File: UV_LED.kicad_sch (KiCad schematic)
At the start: 39 parts, among them IC1 IS31LT3178-GRLS4-TR, J1 Conn_01x04, J2 Conn_01x04

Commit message: added kicad files
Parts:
- removed D13, D16, D17, D18, D19, D6: LED, symbol Device:LED
- removed U?: (no value), symbol LED:CN5501
- removed U?: CN5501, symbol LED:CN5501
- added Q1, Q2: Q_NMOS_GDS, Package_TO_SOT_SMD:SOT-23, symbol Device:Q_NMOS_GDS
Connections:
- net at D5.1 (K), R2.1: now also Q1.2 (D)
- net at C1.1, IC1.1 (OUT_1), IC1.2 (OUT_2): now also Q1.3 (S), Q2.3 (S)
- net at D12.1 (K): now also Q2.2 (D)
- net at R1.2: now also Q1.1 (G)
- net at R2.2: now also Q2.1 (G)

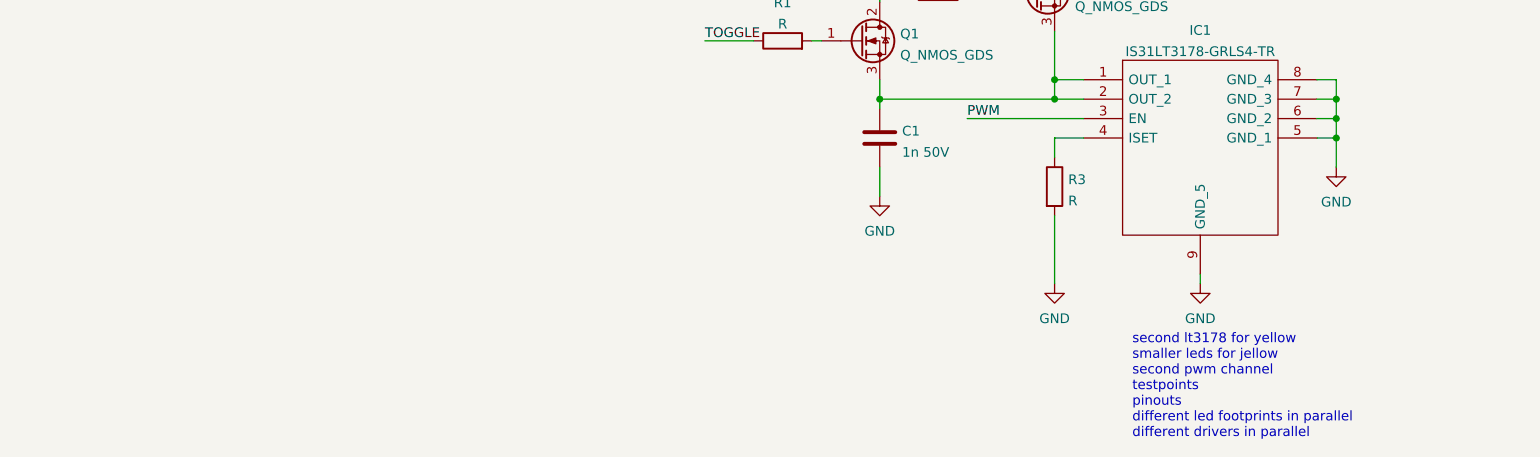
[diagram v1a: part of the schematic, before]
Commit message: added TX6120, CN5501 and AL8861
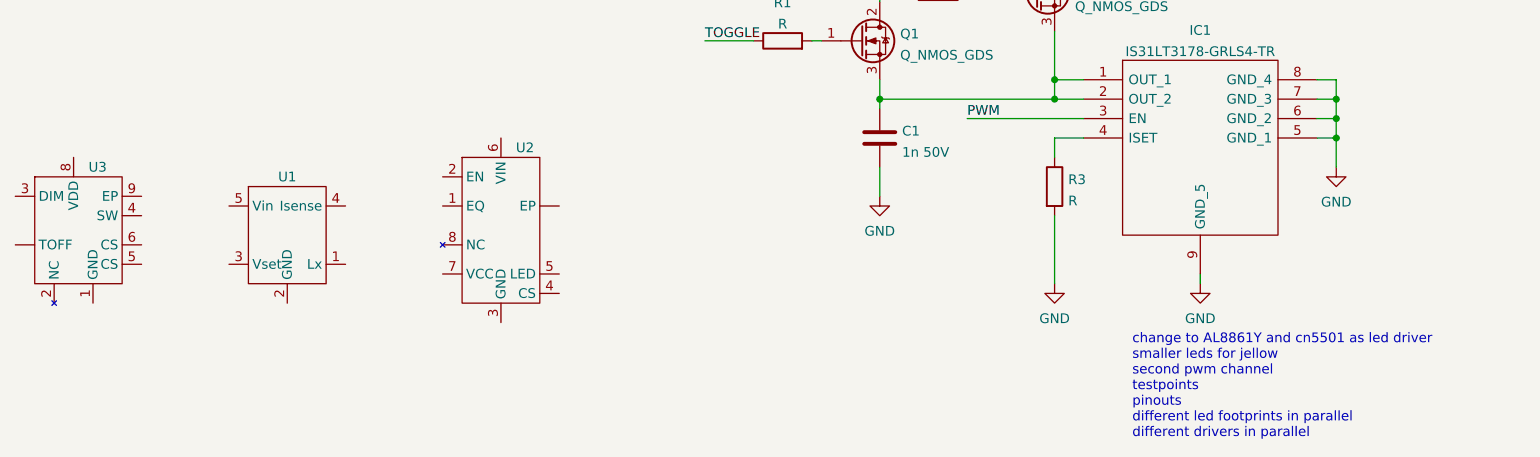
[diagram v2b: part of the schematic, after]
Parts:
- added U1: ~, symbol 1_meins:AL8861
- added U2: ~, symbol 1_meins:CN5501
- added U3: ~, symbol 1_meins:TX6120
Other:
- note added: "change to AL8861Y and cn5501 as led driver smaller leds for jellow second pwm channel testpoints pinouts different led footprints in parallel different drivers in parallel"
- note removed: "second lt3178 for yellow smaller leds for jellow second pwm channel testpoints pinouts different led footprints in parallel different drivers in parallel"

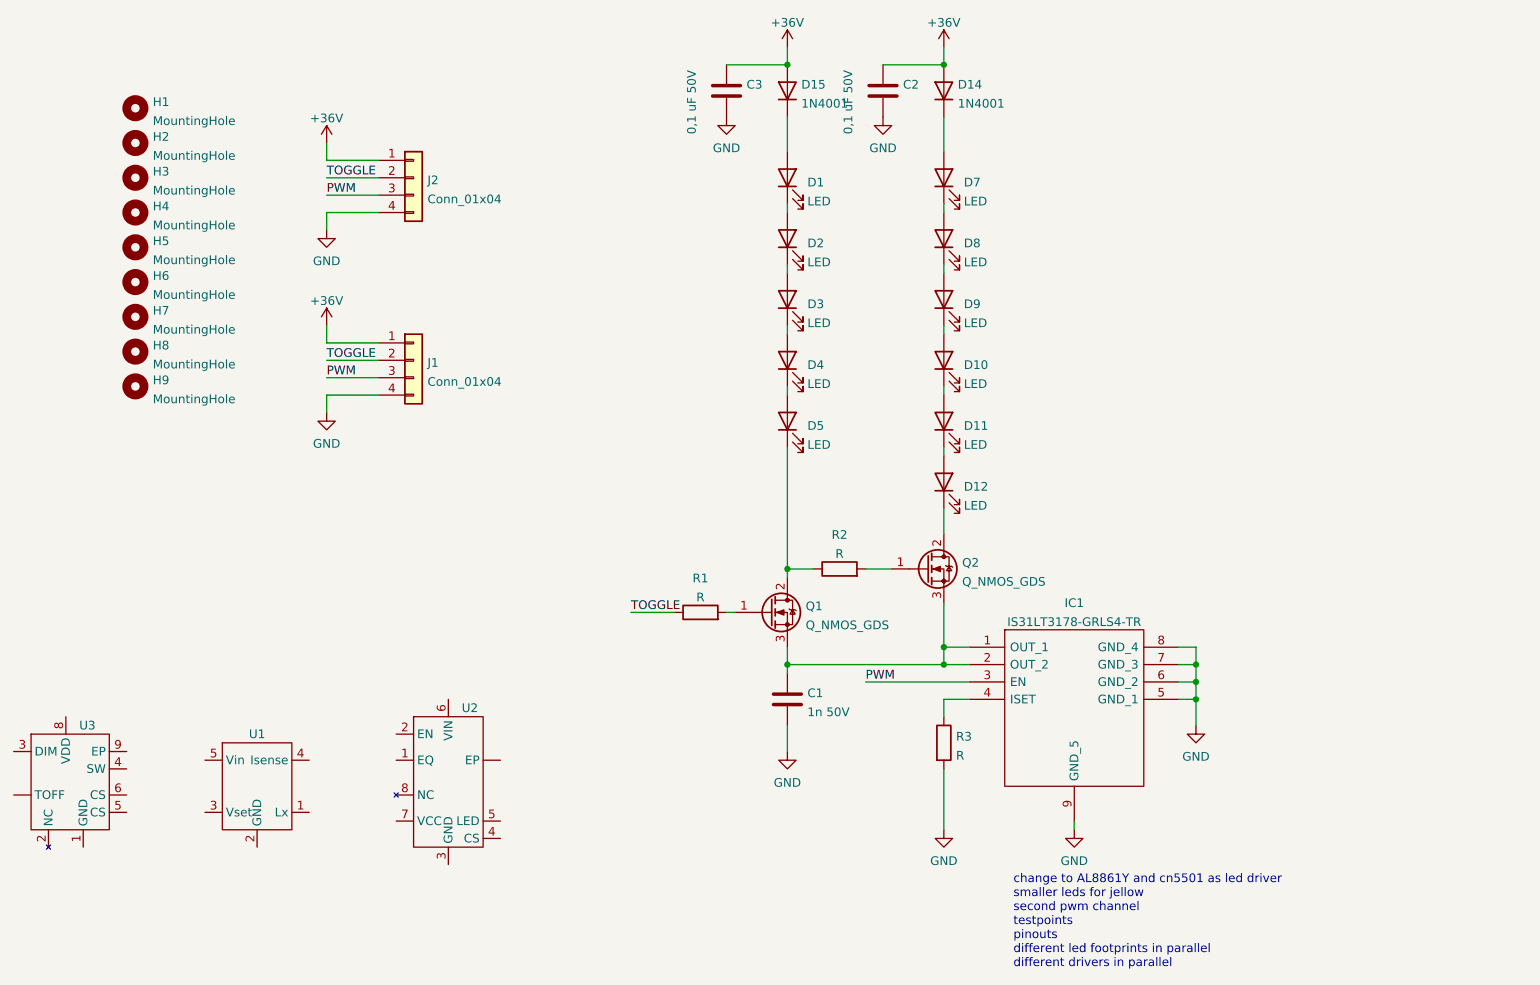
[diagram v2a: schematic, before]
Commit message: sheet for new LED driver
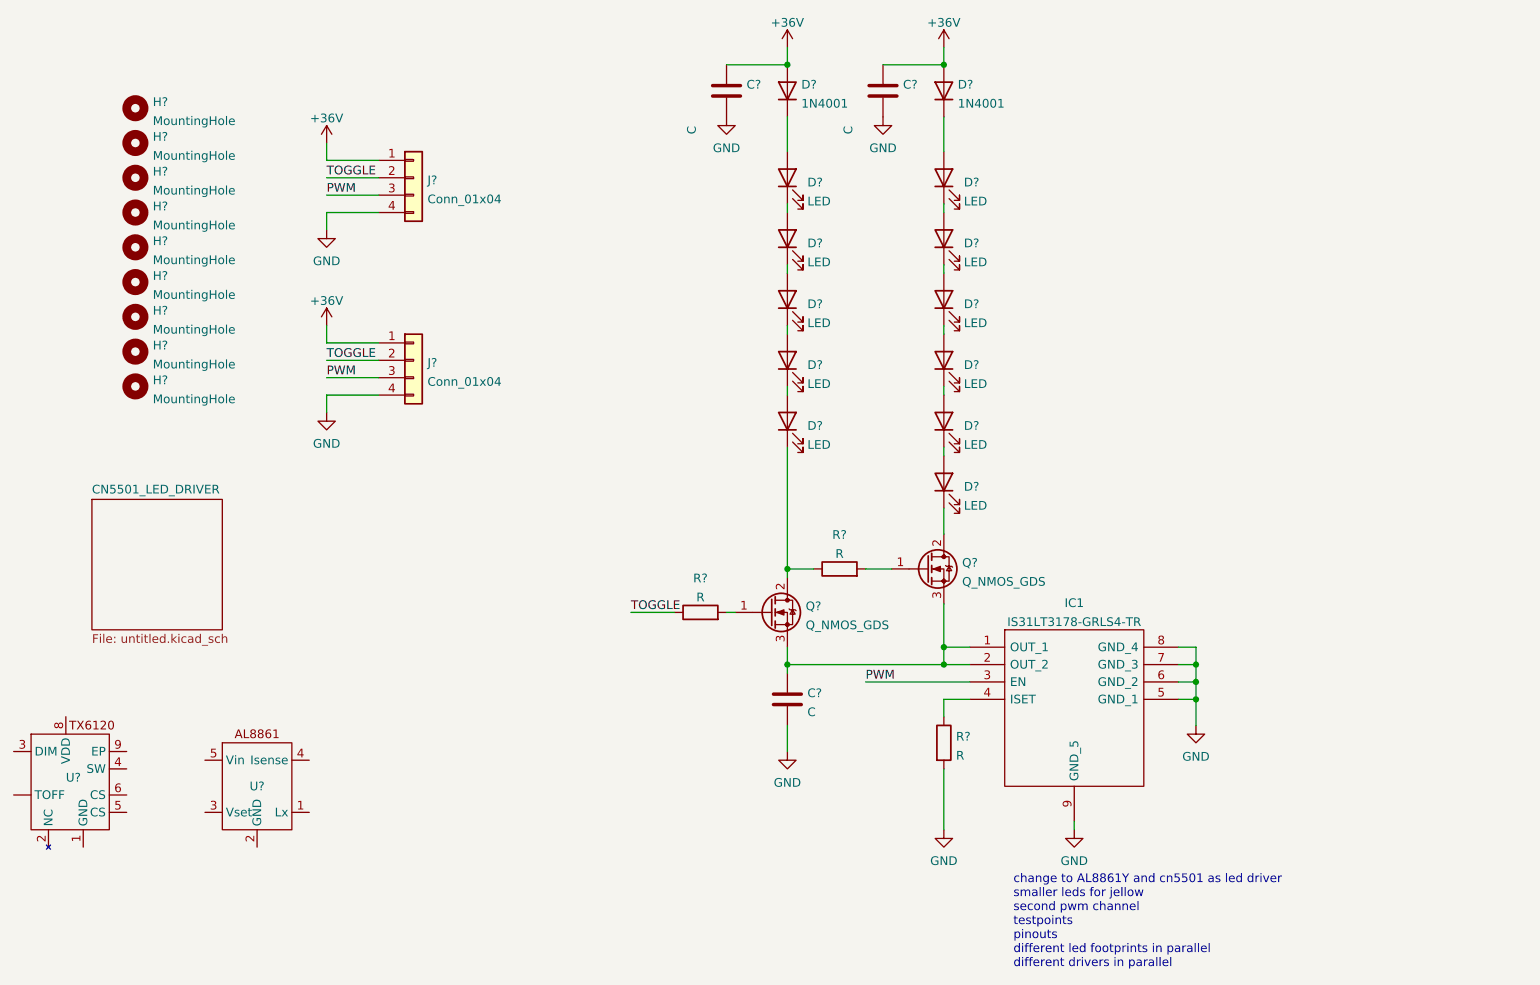
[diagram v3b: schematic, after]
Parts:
- removed U2: ~, symbol 1_meins:CN5501
- C?: renamed from C2; value 0,1 uF 50V -> C
- C?: renamed from C1; value 1n 50V -> C
- C?: renamed from C3; value 0,1 uF 50V -> C
- D?: renamed from D14; footprint Diode_SMD:D_SMA -> Diode_THT:D_DO-41_SOD81_P10.16mm_Horizontal
- D?: renamed from D15; footprint Diode_SMD:D_SMA -> Diode_THT:D_DO-41_SOD81_P10.16mm_Horizontal
- renumbered D5 to D?, D1 to D?, D9 to D?, D8 to D?, D3 to D?, D7 to D?, D11 to D?, D12 to D?, D10 to D?, D2 to D?, D4 to D?, H7 to H?, H8 to H?, H4 to H?, H6 to H?, H9 to H?, H2 to H?, H3 to H?, H5 to H?, H1 to H?, J2 to J?, J1 to J?, Q1 to Q?, Q2 to Q?, R1 to R?, R3 to R?, R2 to R?, U1 to U?, U3 to U?
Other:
- added sheet CN5501_LED_DRIVER (untitled.kicad_sch)

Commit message: finalised layout
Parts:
- removed C? (x3): C, Capacitor_SMD:C_1206_3216Metric, symbol Device:C
- removed D? (x7): LED, LED_SMD:LED_1W_3W_R8, symbol Device:LED
- removed D? (x2): 1N4001, Diode_THT:D_DO-41_SOD81_P10.16mm_Horizontal, symbol Diode:1N4001
- removed IC1: IS31LT3178-GRLS4-TR, Package_SO:HSOP-8-1EP_3.9x4.9mm_P1.27mm_EP2.41x3.1mm, symbol IS31LT3178-GRLS4-TR:IS31LT3178-GRLS4-TR
- removed Q?: Q_NMOS_GDS, Package_TO_SOT_SMD:SOT-23, symbol Device:Q_NMOS_GDS
- removed R? (x3): R, Resistor_SMD:R_1206_3216Metric, symbol Device:R
- removed U?: ~, symbol 1_meins:AL8861
- removed U?: ~, symbol 1_meins:TX6120
- added C3: C, Capacitor_SMD:C_1206_3216Metric_Pad1.33x1.80mm_HandSolder, symbol Device:C
- added D10, D11, D8, D9: LED_Pad, meins:UV_3535, symbol Device:LED_Pad
- added R3: R, Resistor_SMD:R_2512_6332Metric_Pad1.40x3.35mm_HandSolder, symbol Device:R
- added R4: R, Resistor_SMD:R_0603_1608Metric_Pad0.98x0.95mm_HandSolder, symbol Device:R
- added TP1, TP2, TP3, TP4, TP5: TestPoint, TestPoint:TestPoint_THTPad_2.0x2.0mm_Drill1.0mm, symbol Connector:TestPoint
- D2, D3, D4, D5: renamed from D?; footprint LED_SMD:LED_1W_3W_R8 -> LED_SMD:LED_1210_3225Metric_Pad1.42x2.65mm_HandSolder
- Q1: renamed from Q?; value Q_NMOS_GDS -> Q_NMOS_GSD; symbol Device:Q_NMOS_GDS -> Device:Q_NMOS_GSD
- gave numbers to parts that had none: 11
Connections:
- net +36V: now also R3.2
- net GND: now also Q1.2 (S)
- net PWM: now also TP5.1
- net TOGGLE: now also R4.1, TP1.1
- net at D5.1 (K): now also Q1.3 (D), TP3.1
- net at D2.2 (A): now also R3.1
- net at Q1.1 (G): now also R4.2, TP2.1
- new net: D8.2 (A), D9.1 (K)
- new net: D10.1 (K), D9.2 (A)
- new net: D10.2 (A), D11.1 (K)
- new net UV_LED+: C3.1, D11.2 (A)
- new net UV_LED-: C3.2, D8.1 (K), TP4.1
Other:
- removed sheet CN5501_LED_DRIVER
- added sheet AL8861_LED_DRIVER (AL8861_LED_DRIVER.kicad_sch)
- note added: "x change to AL8861Y and cn5501 as led driver smaller leds for jellow second pwm channel x testpoints pinouts ? different led footprints in parallel x different drivers in parallel"
- note removed: "change to AL8861Y and cn5501 as led driver smaller leds for jellow second pwm channel testpoints pinouts different led footprints in parallel different drivers in parallel"
